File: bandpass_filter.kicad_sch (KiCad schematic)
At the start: 22 parts, among them J1 PCB.SMAFRA.HT, J3 PCB.SMAFRA.HT

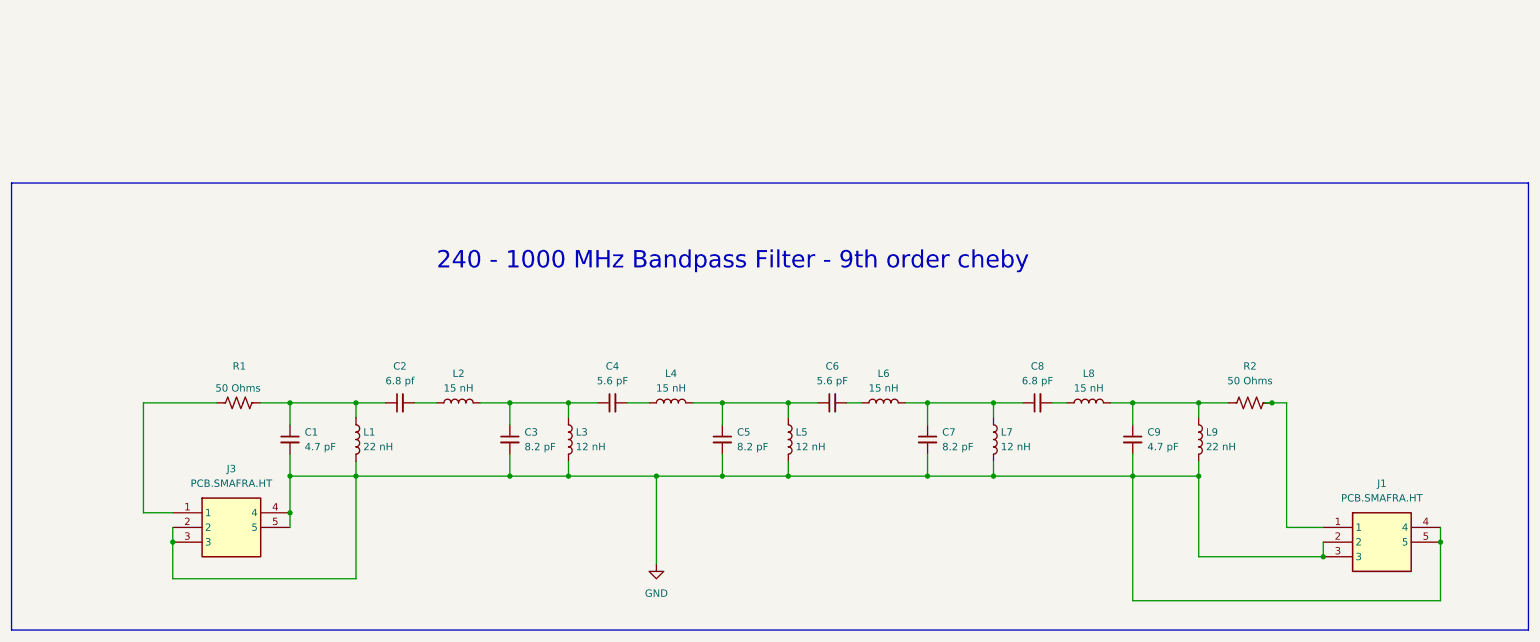
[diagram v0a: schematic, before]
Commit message: Add spice model.
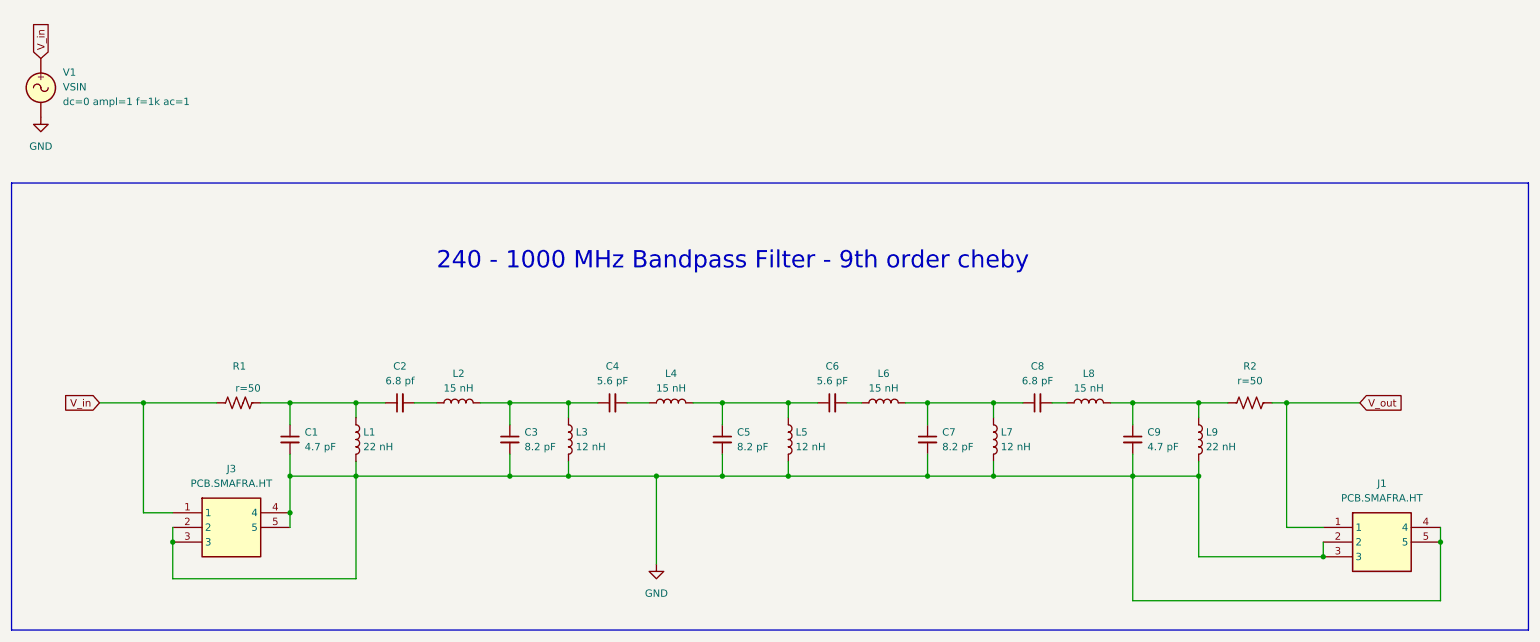
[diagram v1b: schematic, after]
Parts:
- added V1: VSIN, symbol Simulation_SPICE:VSIN
- R1, R2: value 50 Ohms -> ${SIM.PARAMS}
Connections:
- net GND: now also V1.2
- net V_out: now reaches J1.1, R2.2
- net V_in: now reaches J3.1, R1.1
- net V_in: now also V1.1
